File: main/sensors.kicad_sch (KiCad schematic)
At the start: 0 parts

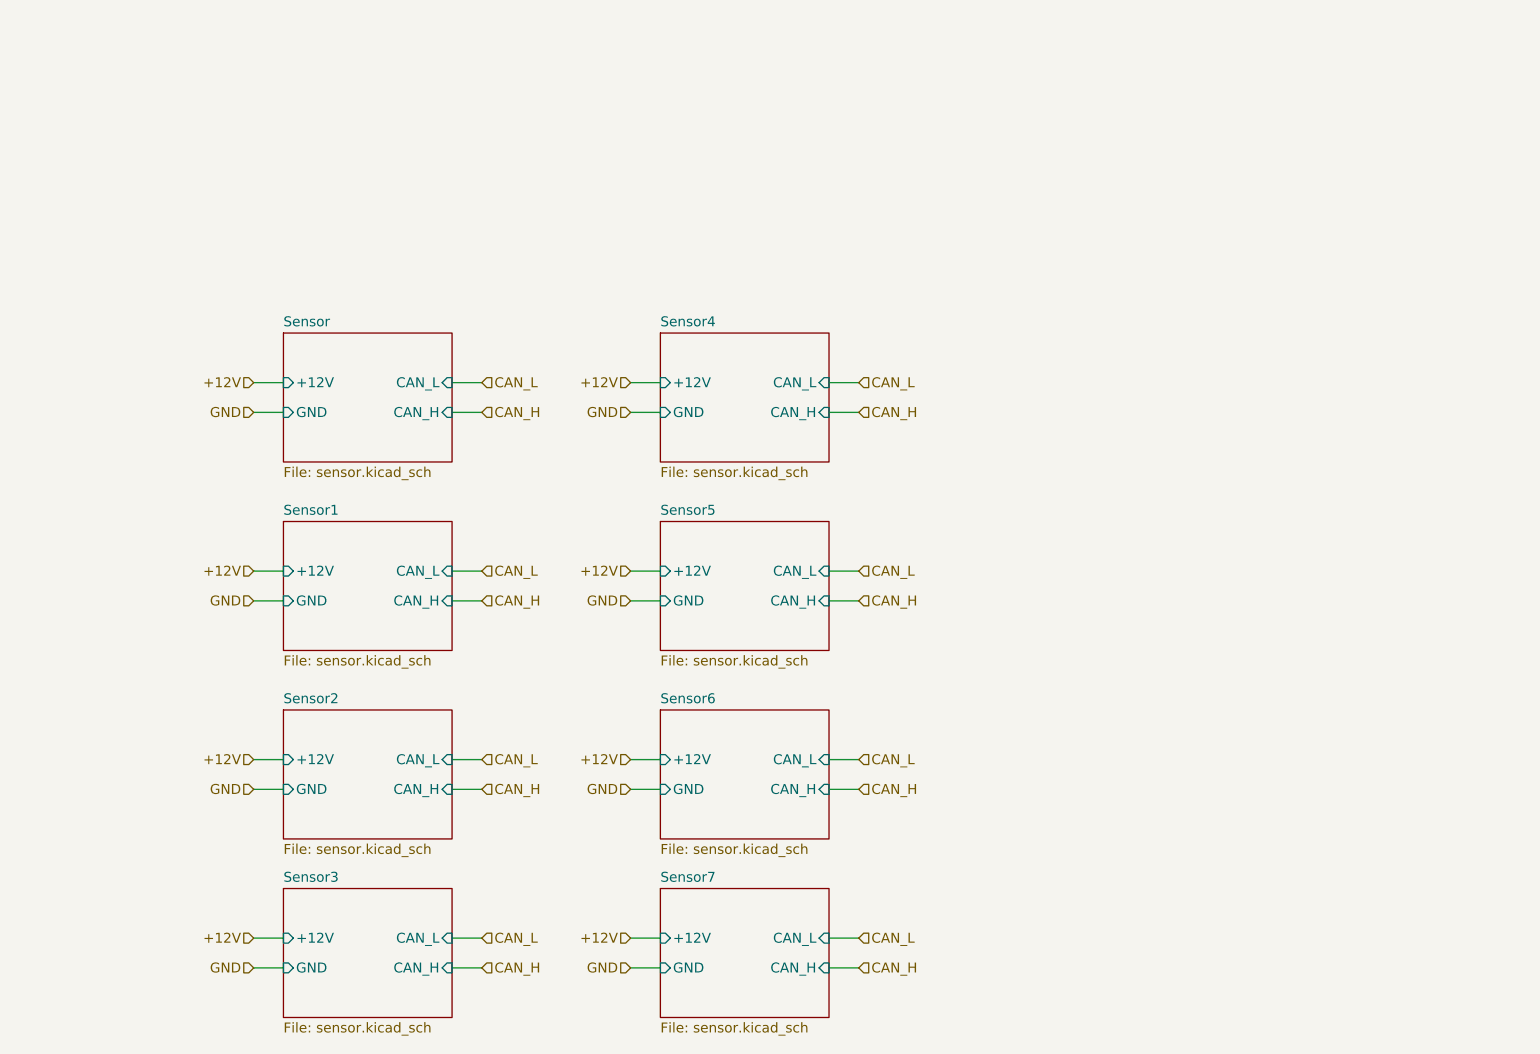
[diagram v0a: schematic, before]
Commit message: Added battery_temp_sensors
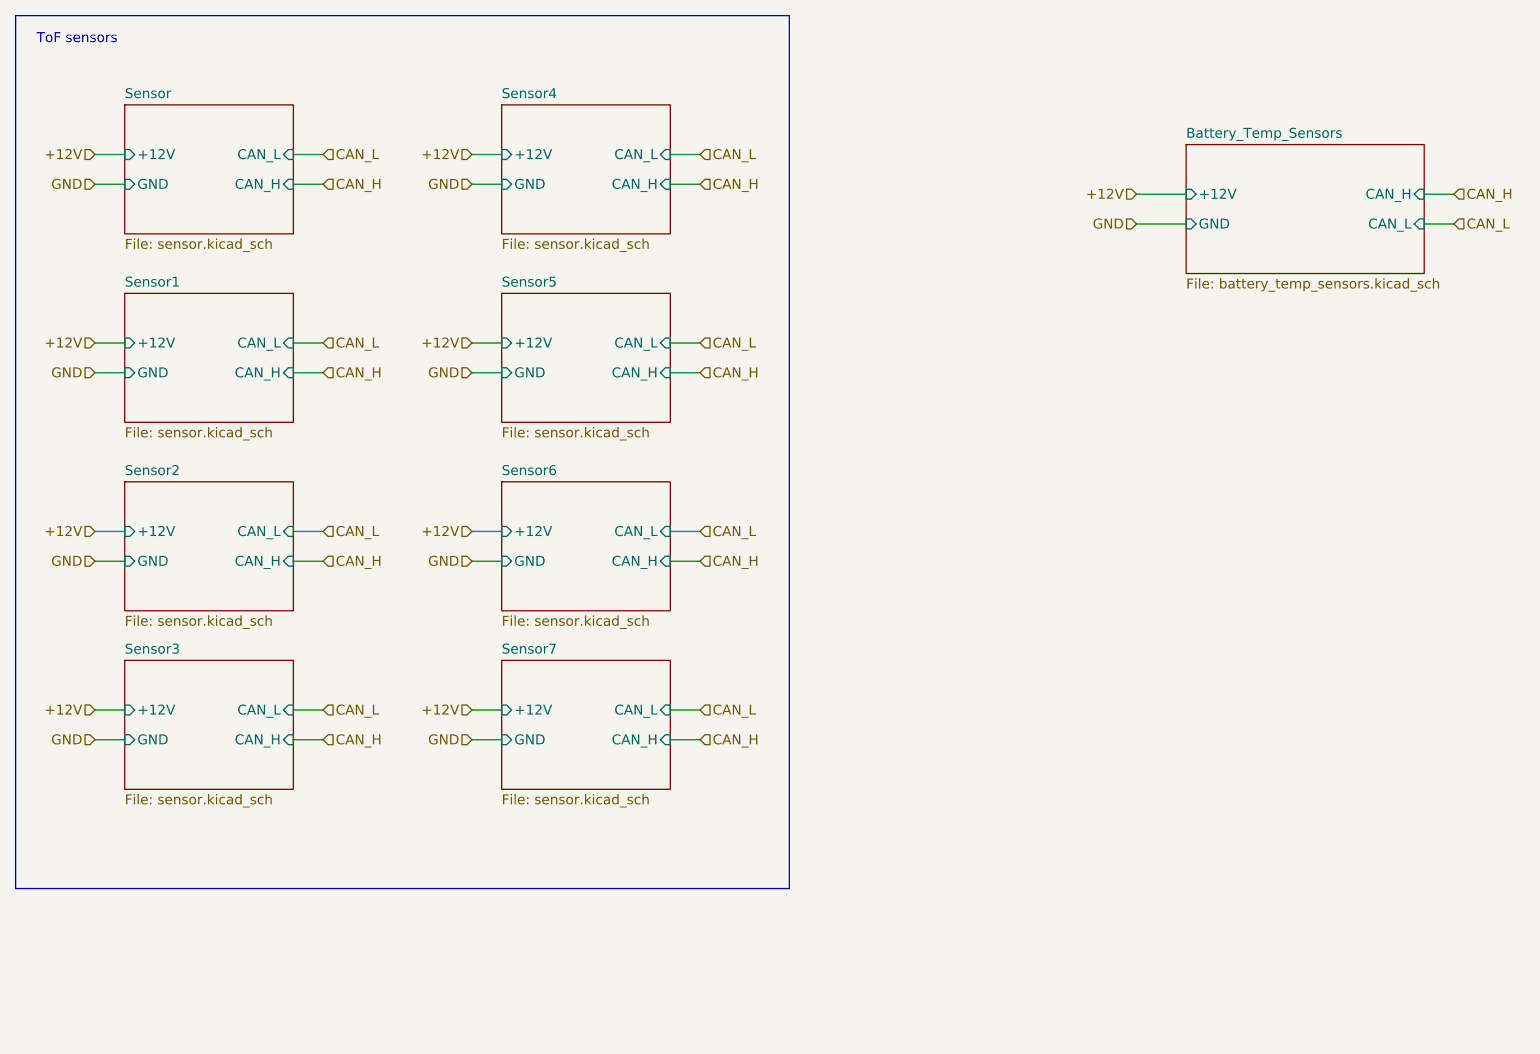
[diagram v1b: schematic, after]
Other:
- added sheet Battery_Temp_Sensors (battery_temp_sensors.kicad_sch)
- note added: "ToF sensors"

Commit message: added logos, oranised sheets, final version
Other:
- company: (none) -> Designers: Krzysztof Grajek, Wojtek Kołodziej
- title: (none) -> Sensors schematic
